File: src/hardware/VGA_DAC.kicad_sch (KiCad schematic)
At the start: 22 parts, among them J501 VGA OUT

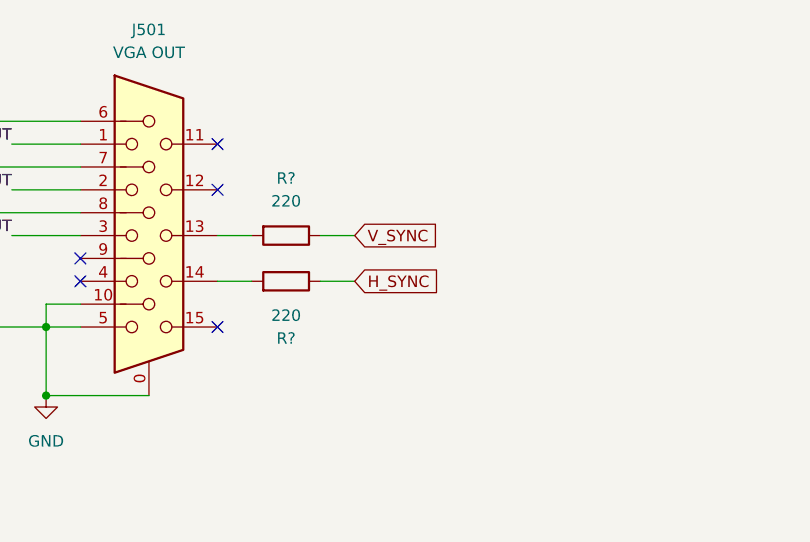
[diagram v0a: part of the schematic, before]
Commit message: Fixed sync pin mixup - Rev 2.0
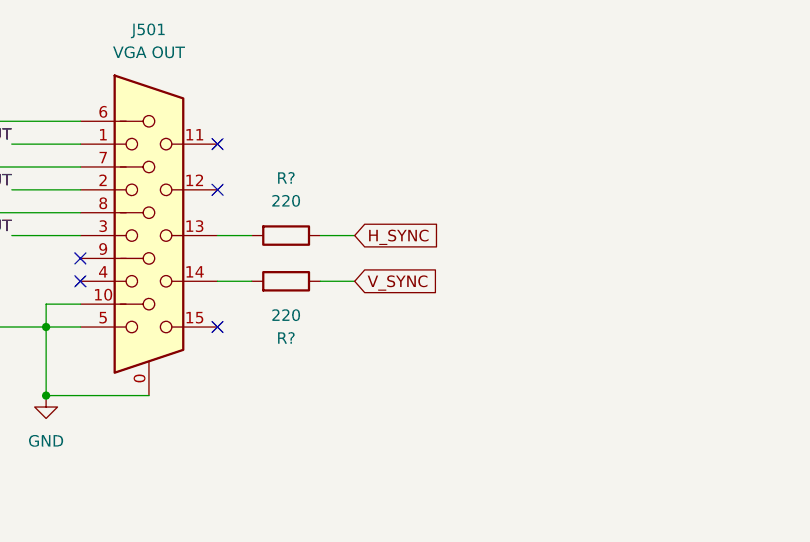
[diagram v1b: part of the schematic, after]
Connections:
- net H_SYNC: now also R?.1; no longer R?.1
- net V_SYNC: now also R?.1; no longer R?.1
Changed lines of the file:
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@@
     (effects (font (size 1.27 1.27)) (justify left bottom))
-  )
-  (global_label "V_SYNC" (shape input) (at 168.91 63.5 0) (fields_autoplaced)
-    (effects (font (size 1.27 1.27)) (justify left))
-    (property "Intersheetrefs" "${INTERSHEET_REFS}" (at 178.85 63.5 0)
-      (effects (font (size 1.27 1.27)) (justify left) hide)
-    )
-  )
-  (global_label "H_SYNC" (shape input) (at 168.91 68.58 0) (fields_autoplaced)
-    (effects (font (size 1.27 1.27)) (justify left))
-    (property "Intersheetrefs" "${INTERSHEET_REFS}" (at 179.0919 68.58 0)
-      (effects (font (size 1.27 1.27)) (justify left) hide)
-    )
   )
   (global_label "RED[1..3]" (shape input) (at 45.72 105.41 180) (fields_autoplaced)
@@
     )
   )
+  (global_label "V_SYNC" (shape input) (at 168.91 68.58 0) (fields_autoplaced)
+    (effects (font (size 1.27 1.27)) (justify left))
+    (property "Intersheetrefs" "${INTERSHEET_REFS}" (at 178.85 68.58 0)
+      (effects (font (size 1.27 1.27)) (justify left) hide)
+    )
+  )
   (global_label "BLUE[1..2]" (shape input) (at 217.17 105.41 180) (fields_autoplaced)
     (effects (font (size 1.27 1.27)) (justify right))
@@
     )
   )
+  (global_label "H_SYNC" (shape input) (at 168.91 63.5 0) (fields_autoplaced)
+    (effects (font (size 1.27 1.27)) (justify left))
+    (property "Intersheetrefs" "${INTERSHEET_REFS}" (at 179.0919 63.5 0)
+      (effects (font (size 1.27 1.27)) (justify left) hide)
+    )
+  )
